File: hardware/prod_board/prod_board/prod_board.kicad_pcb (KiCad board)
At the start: 2 copper layers, 65.5 x 148 mm, 0 parts

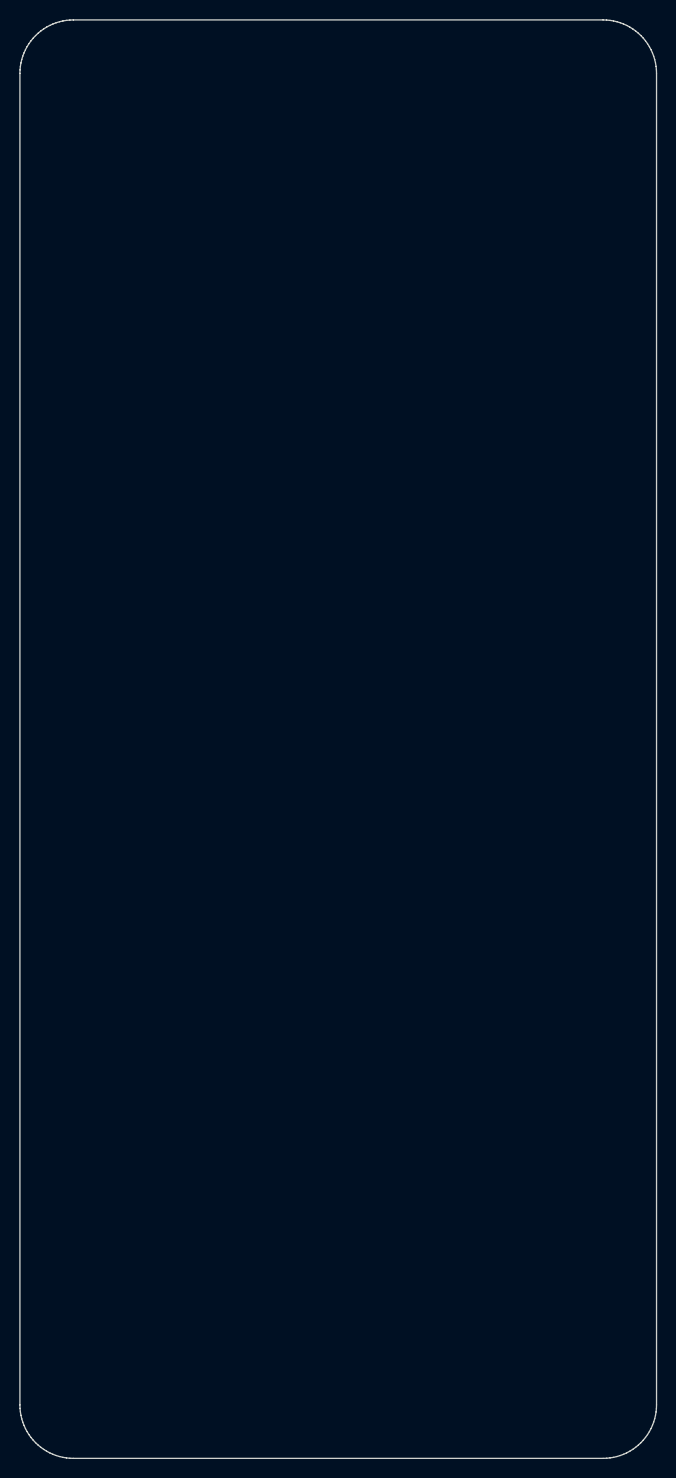
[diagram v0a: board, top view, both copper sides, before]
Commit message: Board: all 16 buttons placed where the case says, and locked
place_buttons.py reads the positions out of the case model's own echo block,
not a copied table, and places DSL_button_4ring at each: SW1 to SW16, seat 1
at the bottom, every one on its target circle from pads.dxf and locked so it
can't be nudged while routing. Re-run it after a case change and every button
moves to its new home. It refuses to run while KiCad has the board open,
since KiCad would overwrite the result on its next save.

The first run placed a second SW1 over the hand-placed one, because KiCad
returns footprint names as its own string type and a plain comparison never
matched. Restored from the backup and re-run with the comparison fixed; DRC is
clean.

Co-Authored-By: Claude Opus 5.5 (1M context) <noreply@anthropic.com>
Claude-Session: https://claude.ai/code/session_01KGgEu3CbFtCsvHRQgAFiCN
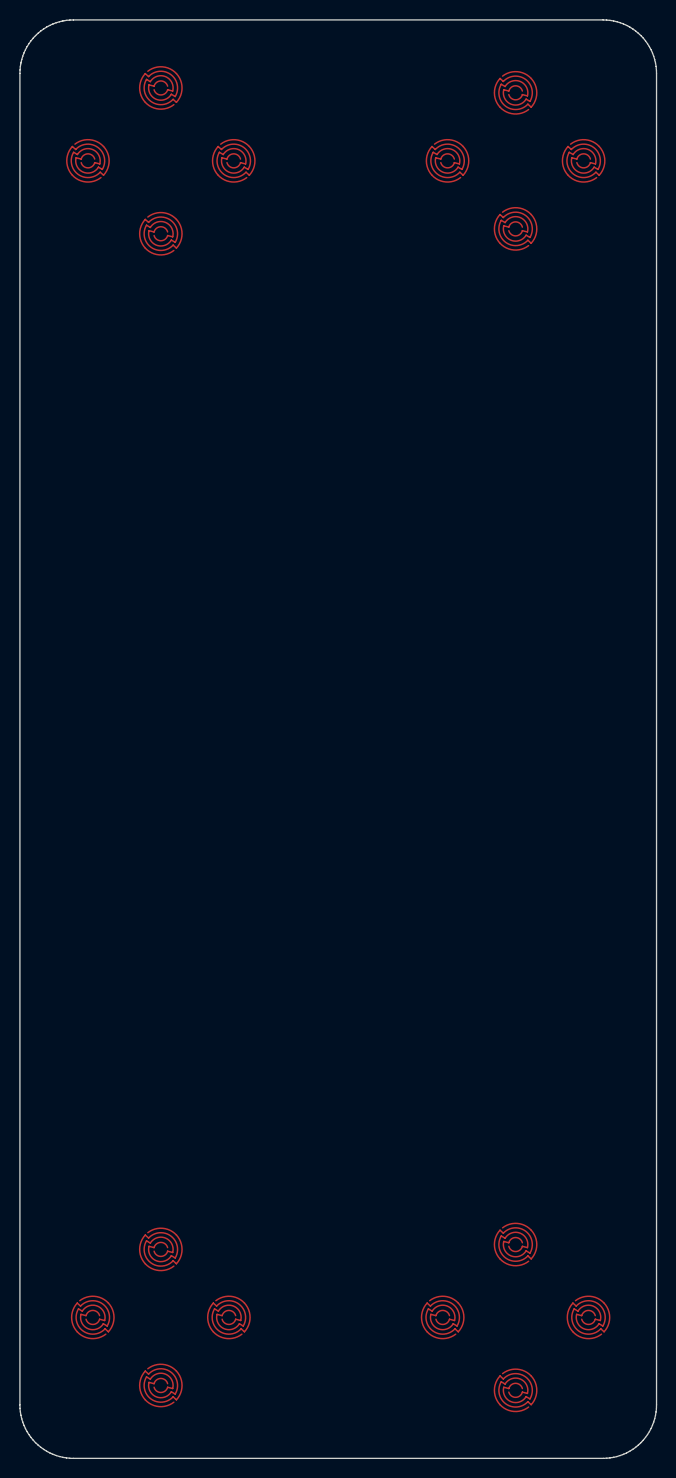
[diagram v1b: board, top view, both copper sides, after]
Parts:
- added SW1: DSL_button_4ring, prod:DSL_button_4ring, F.Cu at (81.8, 152.5)
- added SW10: DSL_button_4ring, prod:DSL_button_4ring, F.Cu at (118.2, 33.5)
- added SW11: DSL_button_4ring, prod:DSL_button_4ring, F.Cu at (125.2, 40.5)
- added SW12: DSL_button_4ring, prod:DSL_button_4ring, F.Cu at (111.2, 40.5)
- added SW13: DSL_button_4ring, prod:DSL_button_4ring, F.Cu at (74.2, 40.5)
- added SW14: DSL_button_4ring, prod:DSL_button_4ring, F.Cu at (81.8, 33.0)
- added SW15: DSL_button_4ring, prod:DSL_button_4ring, F.Cu at (81.8, 48.0)
- added SW16: DSL_button_4ring, prod:DSL_button_4ring, F.Cu at (89.2, 40.5)
- added SW2: DSL_button_4ring, prod:DSL_button_4ring, F.Cu at (81.8, 166.5)
- added SW3: DSL_button_4ring, prod:DSL_button_4ring, F.Cu at (74.8, 159.5)
- added SW4: DSL_button_4ring, prod:DSL_button_4ring, F.Cu at (88.8, 159.5)
- added SW5: DSL_button_4ring, prod:DSL_button_4ring, F.Cu at (125.8, 159.5)
- added SW6: DSL_button_4ring, prod:DSL_button_4ring, F.Cu at (118.2, 167.0)
- added SW7: DSL_button_4ring, prod:DSL_button_4ring, F.Cu at (118.2, 152.0)
- added SW8: DSL_button_4ring, prod:DSL_button_4ring, F.Cu at (110.8, 159.5)
- added SW9: DSL_button_4ring, prod:DSL_button_4ring, F.Cu at (118.2, 47.5)
